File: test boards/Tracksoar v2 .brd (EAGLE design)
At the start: 50.4 x 19.6 mm, 57 parts, among them IC1 BME280, Y1 16MHZ

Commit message: Schematic cleanup
first pass at making the schematic more readable. Moved components to be more in line with the board layout.
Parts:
- J1: value (none) -> battery
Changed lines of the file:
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@@
 <grid distance="0.001" unitdist="inch" unit="inch" style="lines" multiple="1" display="yes" altdistance="0.025" altunitdist="inch" altunit="mm"/>
 <layers>
-<layer number="1" name="Top" color="4" fill="1" visible="no" active="yes"/>
-<layer number="2" name="Route2" color="6" fill="1" visible="no" active="yes"/>
+<layer number="1" name="Top" color="4" fill="1" visible="yes" active="yes"/>
+<layer number="2" name="Route2" color="6" fill="1" visible="yes" active="yes"/>
 <layer number="3" name="Route3" color="4" fill="3" visible="no" active="no"/>
 <layer number="4" name="Route4" color="1" fill="4" visible="no" active="no"/>
@@
 <layer number="13" name="Route13" color="4" fill="5" visible="no" active="no"/>
 <layer number="14" name="Route14" color="1" fill="6" visible="no" active="no"/>
-<layer number="15" name="Route15" color="3" fill="1" visible="no" active="yes"/>
+<layer number="15" name="Route15" color="3" fill="1" visible="yes" active="yes"/>
 <layer number="16" name="Bottom" color="1" fill="1" visible="yes" active="yes"/>
 <layer number="17" name="Pads" color="2" fill="1" visible="yes" active="yes"/>
@@
 <attribute name="VALUE" x="7.5946" y="12.5476" size="0.6096" layer="27"/>
 </element>
-<element name="J1" library="SparkFun-Connectors" package="JST-2-PTH" value="" x="10.541" y="21.336" smashed="yes" rot="MR270">
+<element name="J1" library="SparkFun-Connectors" package="JST-2-PTH" value="battery" x="10.541" y="21.336" smashed="yes" rot="MR270">
 <attribute name="PROD_ID" value="CONN-09863" x="10.541" y="21.336" size="1.778" layer="28" rot="MR270" display="off"/>
 <attribute name="SKU" value="PRT-09914" x="10.541" y="21.336" size="1.778" layer="28" rot="MR270" display="off"/>

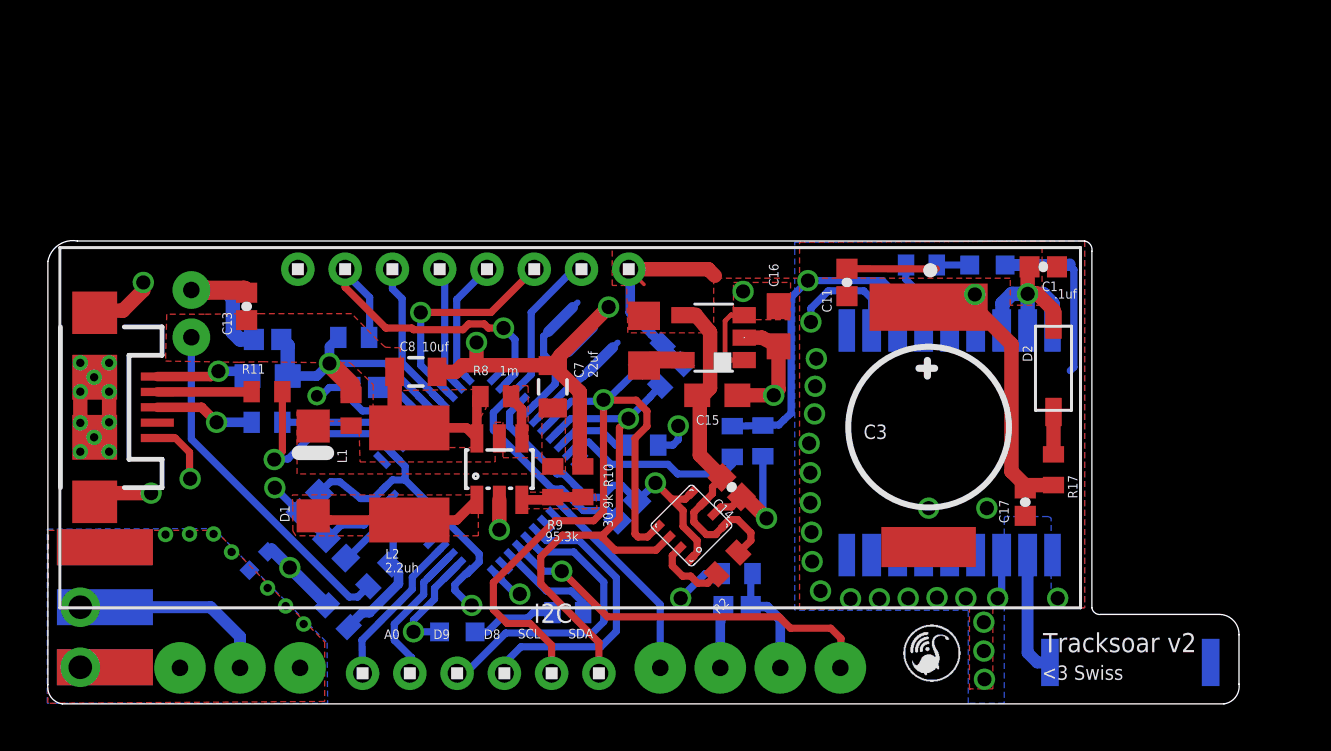
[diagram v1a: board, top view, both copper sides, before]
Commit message: added breakout mount holes
added 2.8mm mounting holes with mouse bites for easy removal.
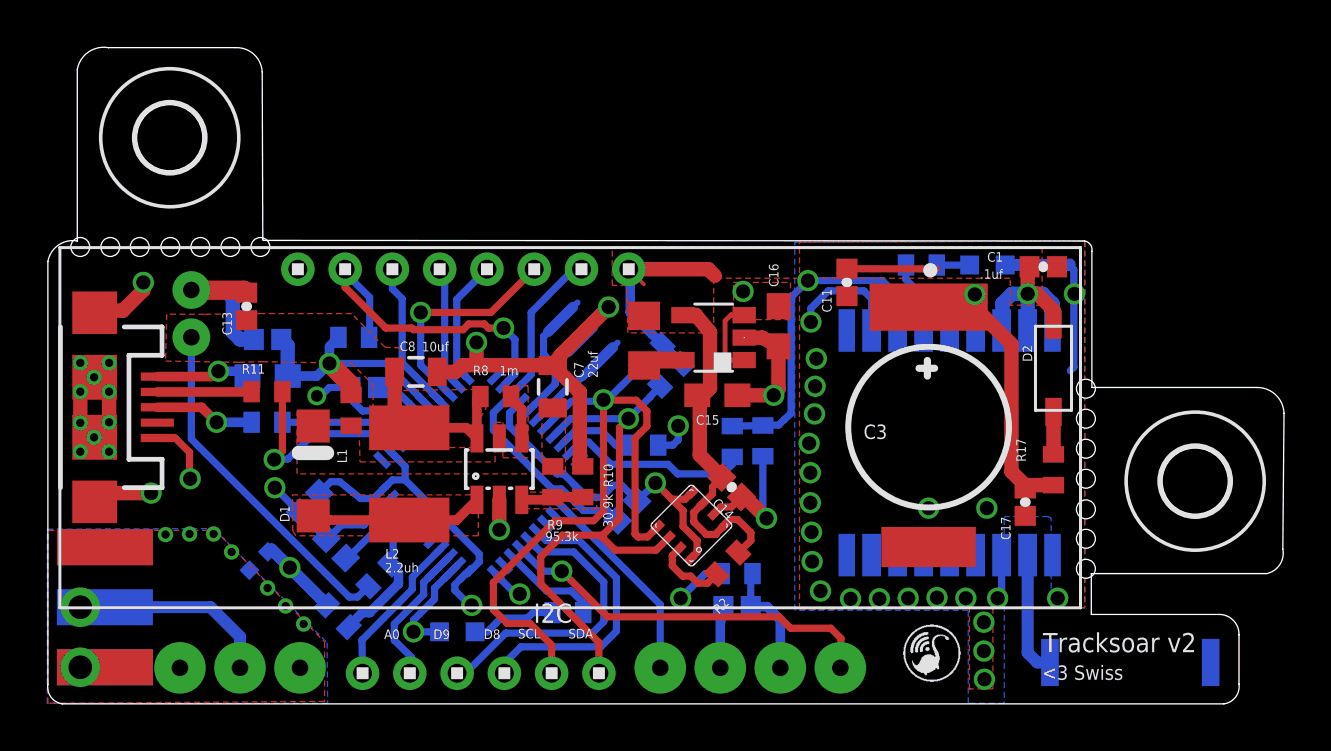
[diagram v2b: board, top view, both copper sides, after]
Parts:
- added H1, H2: MOUNT-HOLE2.8, holes:2,8
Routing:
- net GND: vias 34 -> 35
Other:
- board size 50.4 x 19.6 mm -> 52.3 x 27.8 mm
